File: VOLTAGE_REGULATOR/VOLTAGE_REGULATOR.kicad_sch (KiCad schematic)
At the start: 13 parts, among them J1 Screw_Terminal_01x02, J2 Screw_Terminal_01x02, J3 Screw_Terminal_01x02, U1 L7805, U2 L7809

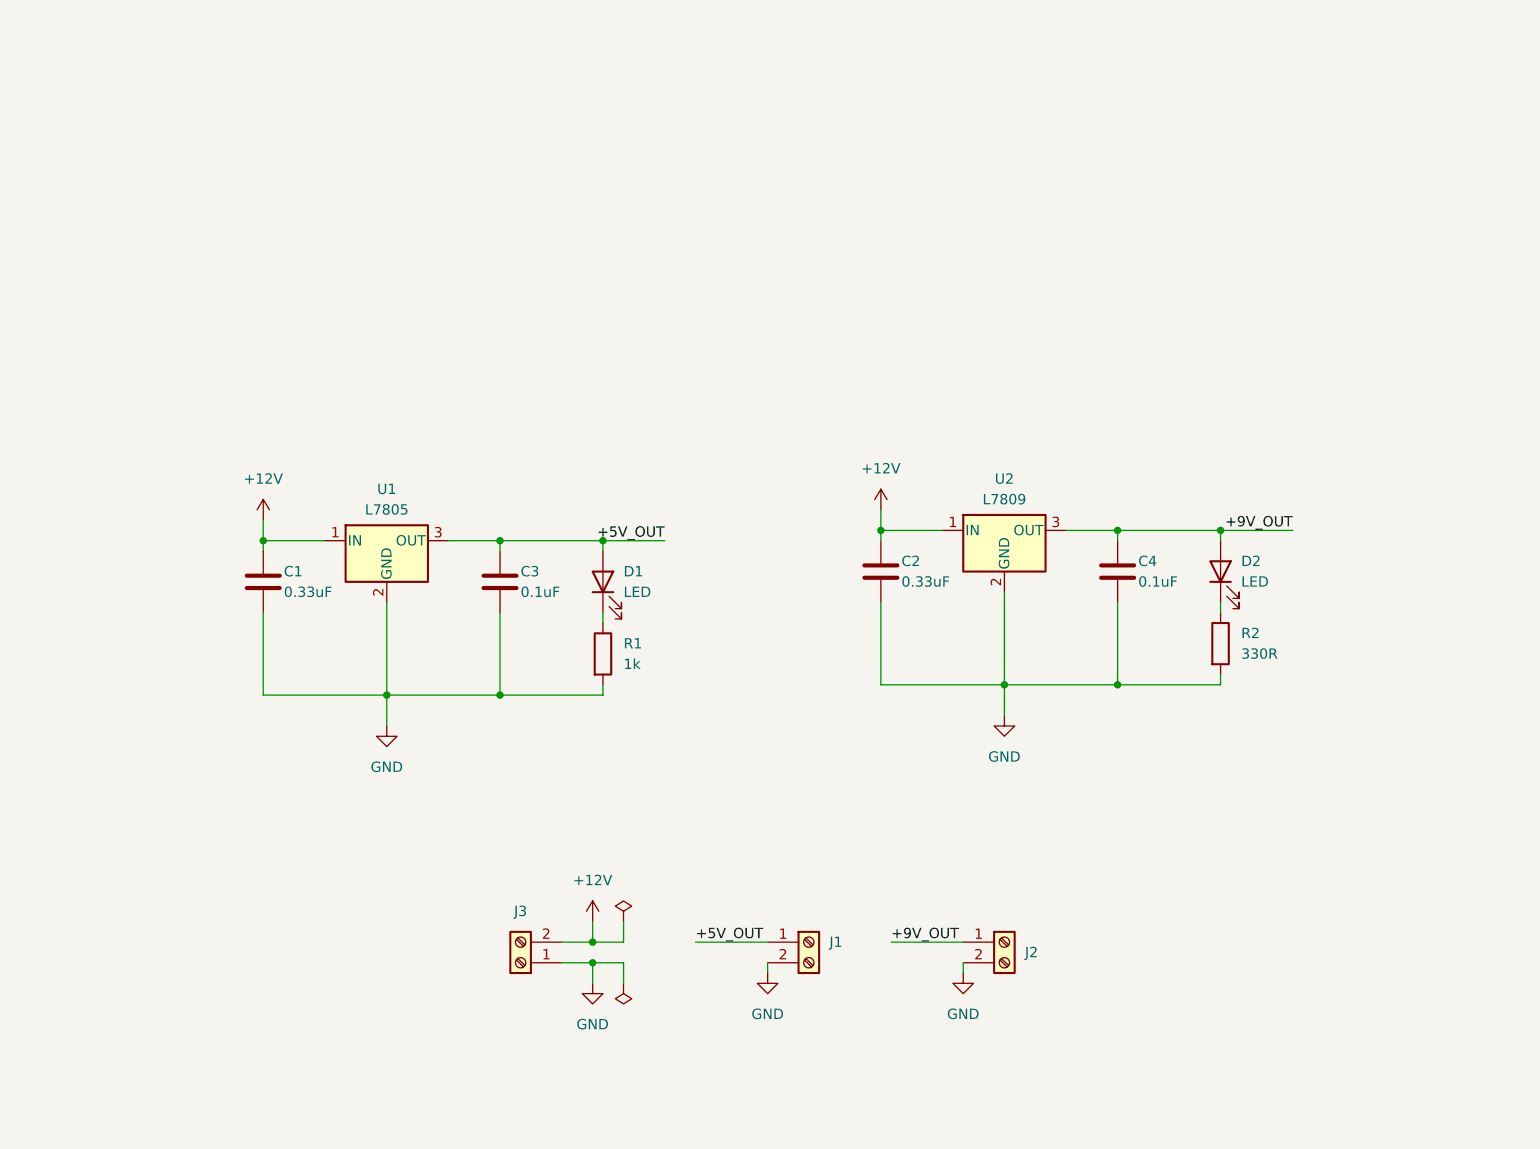
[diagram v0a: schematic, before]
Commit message: voltage regulator(project): add footprints
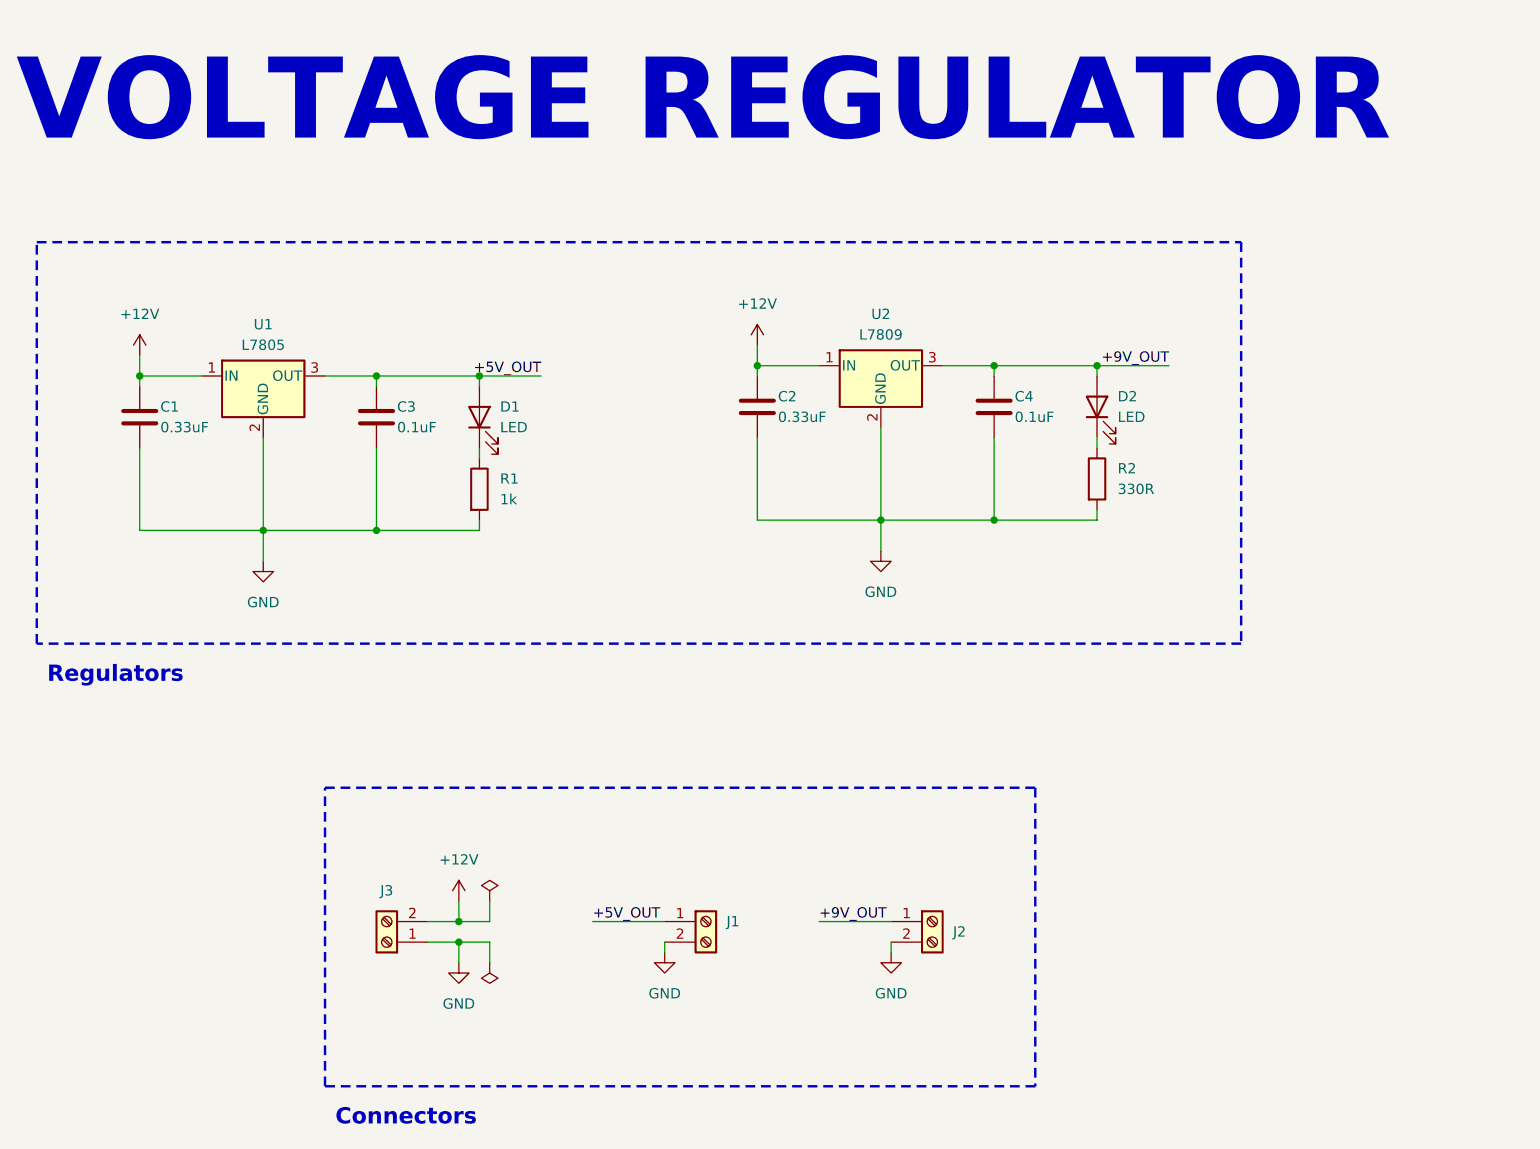
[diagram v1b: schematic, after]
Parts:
- C1, C2: footprint (none) -> Capacitor_THT:C_Disc_D4.7mm_W2.5mm_P5.00mm
- C3, C4: footprint (none) -> Capacitor_THT:C_Disc_D3.0mm_W2.0mm_P2.50mm
- D1, D2: footprint (none) -> LED_THT:LED_D4.0mm
- J1, J2, J3: footprint (none) -> TerminalBlock_Phoenix:TerminalBlock_Phoenix_MKDS-1,5-2-5.08_1x02_P5.08mm_Horizontal
- R1: footprint (none) -> Resistor_THT:R_Axial_DIN0204_L3.6mm_D1.6mm_P5.08mm_Horizontal
- R2: footprint (none) -> Resistor_THT:R_Axial_DIN0207_L6.3mm_D2.5mm_P7.62mm_Horizontal
- U1, U2: footprint (none) -> Package_TO_SOT_THT:TO-220-3_Vertical
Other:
- note added: "Connectors"
- note added: "Regulators"
- note added: "VOLTAGE REGULATOR"
- moved on the sheet: C1, C2, C3, C4, D1, D2, J1, J2, J3, R1, R2, U1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

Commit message: voltage regulator: place components
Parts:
- R1: footprint Resistor_THT:R_Axial_DIN0204_L3.6mm_D1.6mm_P5.08mm_Horizontal -> Resistor_THT:R_Axial_DIN0207_L6.3mm_D2.5mm_P7.62mm_Horizontal
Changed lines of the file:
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@@
       (effects (font (size 1.27 1.27)) (justify left))
     )
-    (property "Footprint" "Resistor_THT:R_Axial_DIN0204_L3.6mm_D1.6mm_P5.08mm_Horizontal" (at 126.492 82.55 90)
+    (property "Footprint" "Resistor_THT:R_Axial_DIN0207_L6.3mm_D2.5mm_P7.62mm_Horizontal" (at 126.492 82.55 90)
       (effects (font (size 1.27 1.27)) hide)
     )
